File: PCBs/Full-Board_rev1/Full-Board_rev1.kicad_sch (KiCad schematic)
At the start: 1 part, among them U1 ESP32-C6-WROOM-1

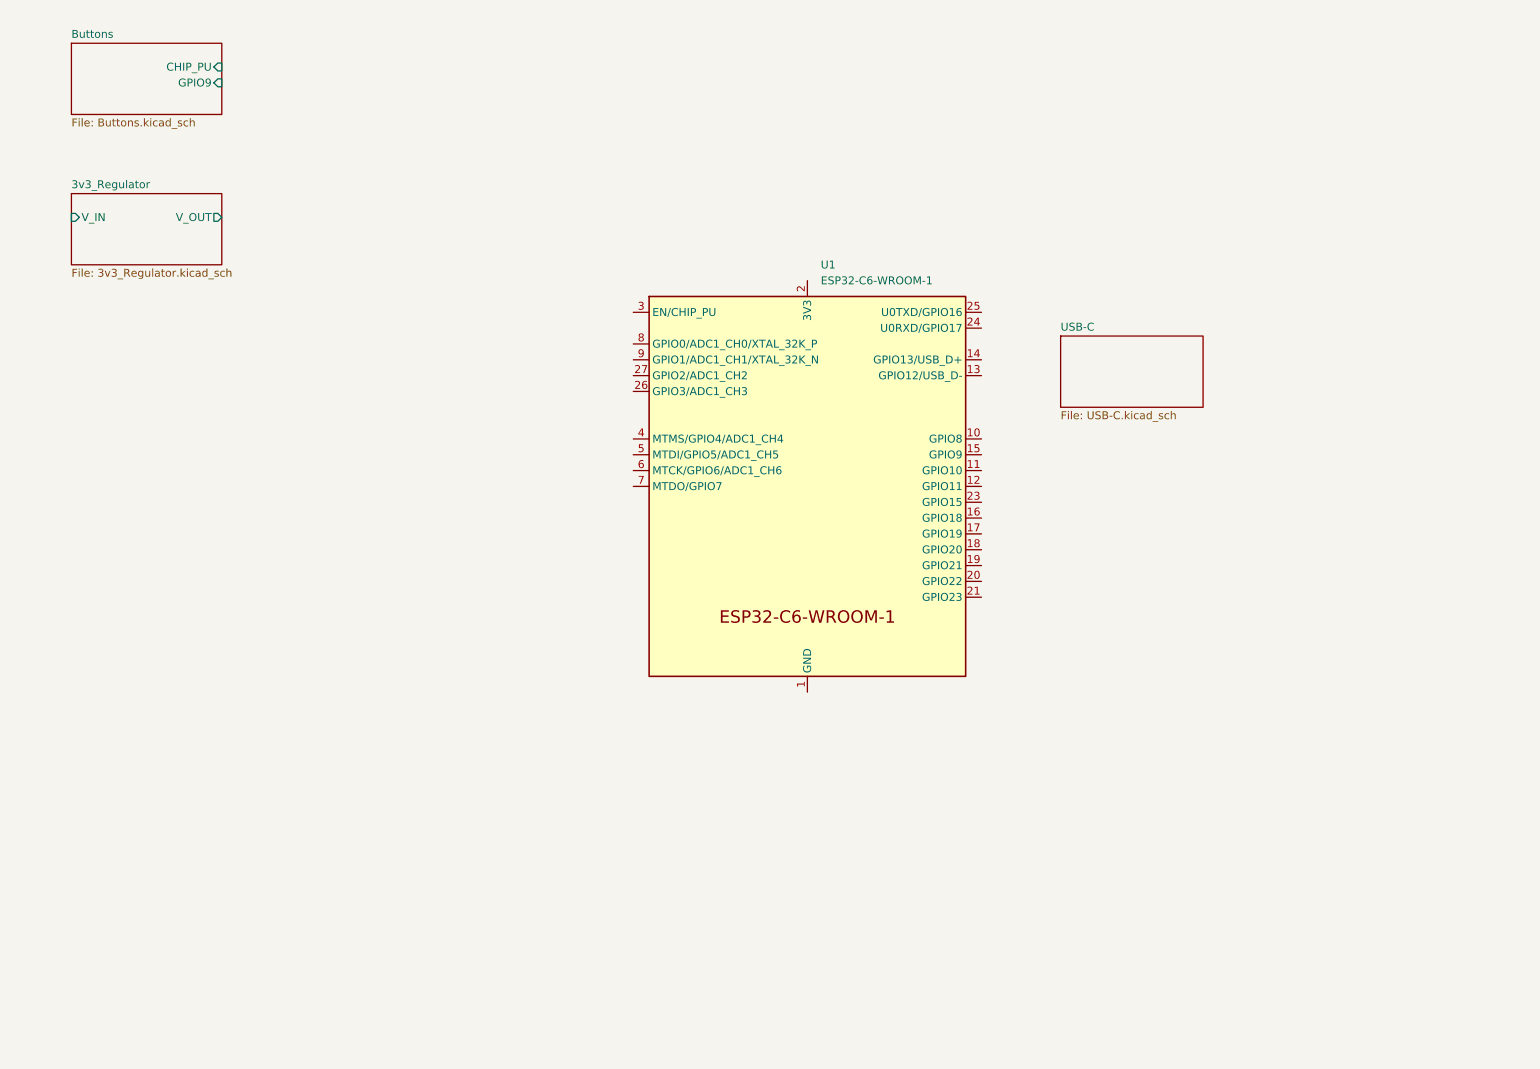
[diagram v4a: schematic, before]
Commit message: added ESP32 peripherals
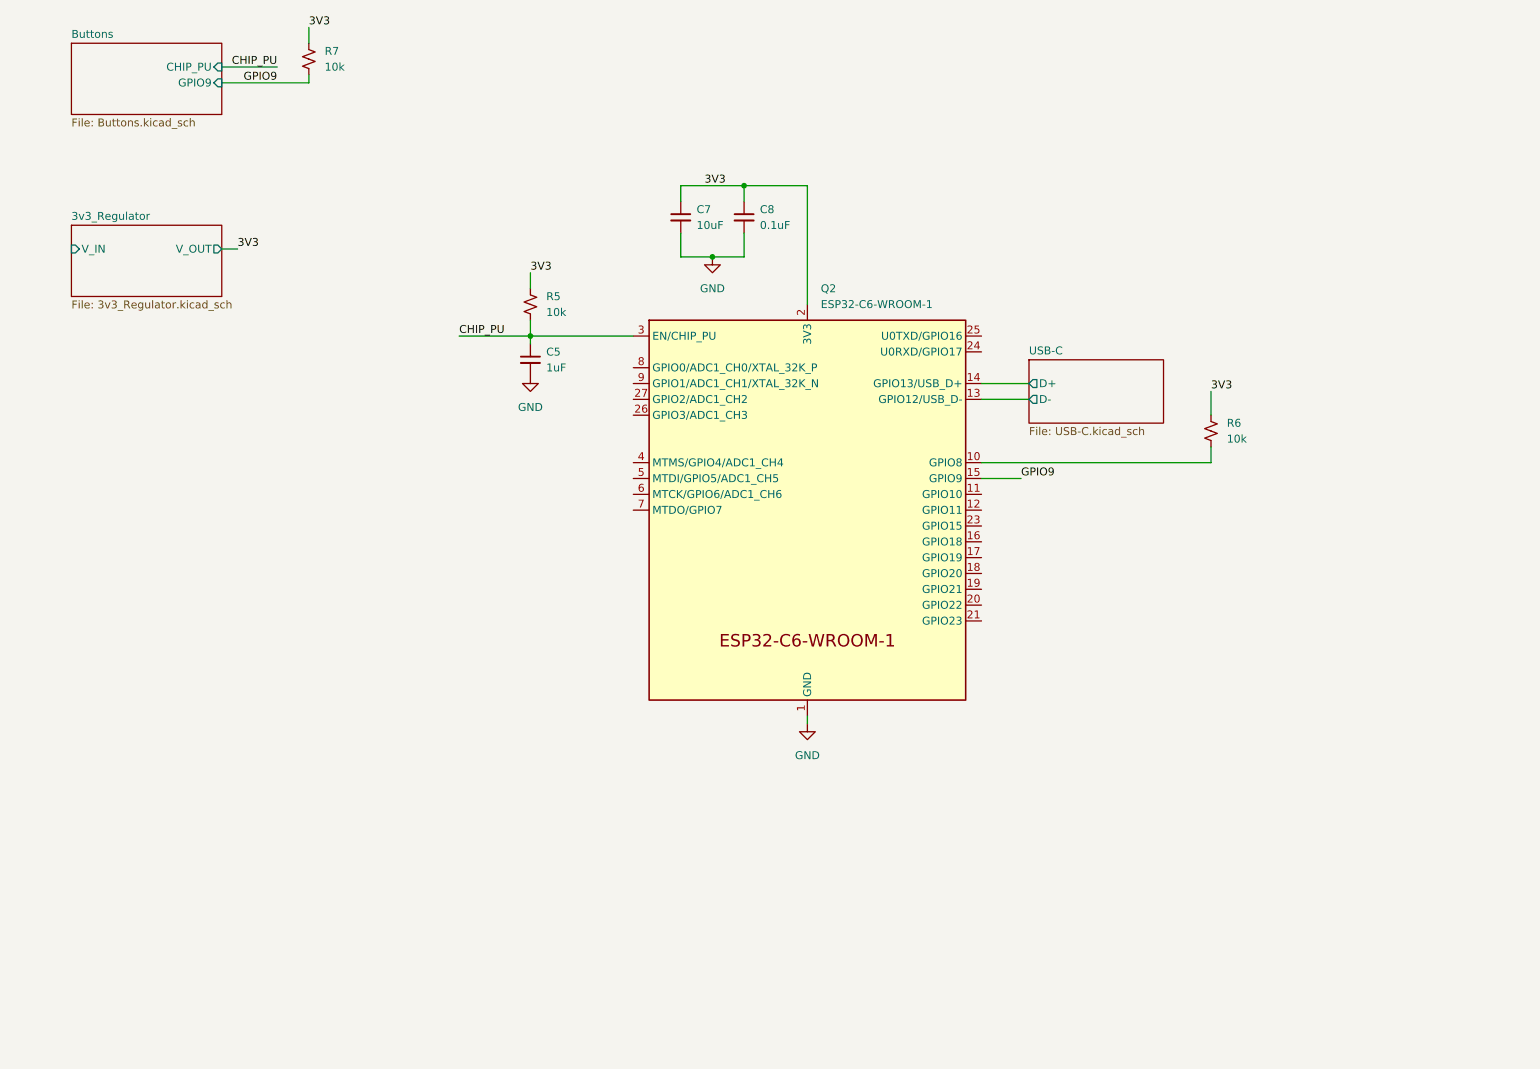
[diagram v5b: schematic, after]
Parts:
- added C5: 1uF, symbol Device:C_Small
- added C7: 10uF, symbol Device:C_Small
- added C8: 0.1uF, symbol Device:C_Small
- added R5, R6, R7: 10k, symbol Device:R_Small_US
- renumbered U1 to Q2
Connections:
- net GND: now reaches Q2.1 (GND), Q2.28 (GND), Q2.29 (GND)
- net GND: now also C5.2, C7.2, C8.2
- net at Q2.10 (GPIO8): now also R6.2
- net USB-C/D-: now reaches Q2.13 (GPIO12/USB_D-)
- net USB-C/D+: now reaches Q2.14 (GPIO13/USB_D+)
- net GPIO9: now reaches Q2.15 (GPIO9)
- net GPIO9: now also R7.2
- net 3V3: now reaches Q2.2 (3V3)
- net 3V3: now also C7.1, C8.1, R5.1, R6.1, R7.1
- net CHIP_PU: now reaches Q2.3 (EN/CHIP_PU)
- net CHIP_PU: now also C5.1, R5.2
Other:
- sheet USB-C ports: added D+, D-; removed none
- moved on the sheet: Q2

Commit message: LEDs added
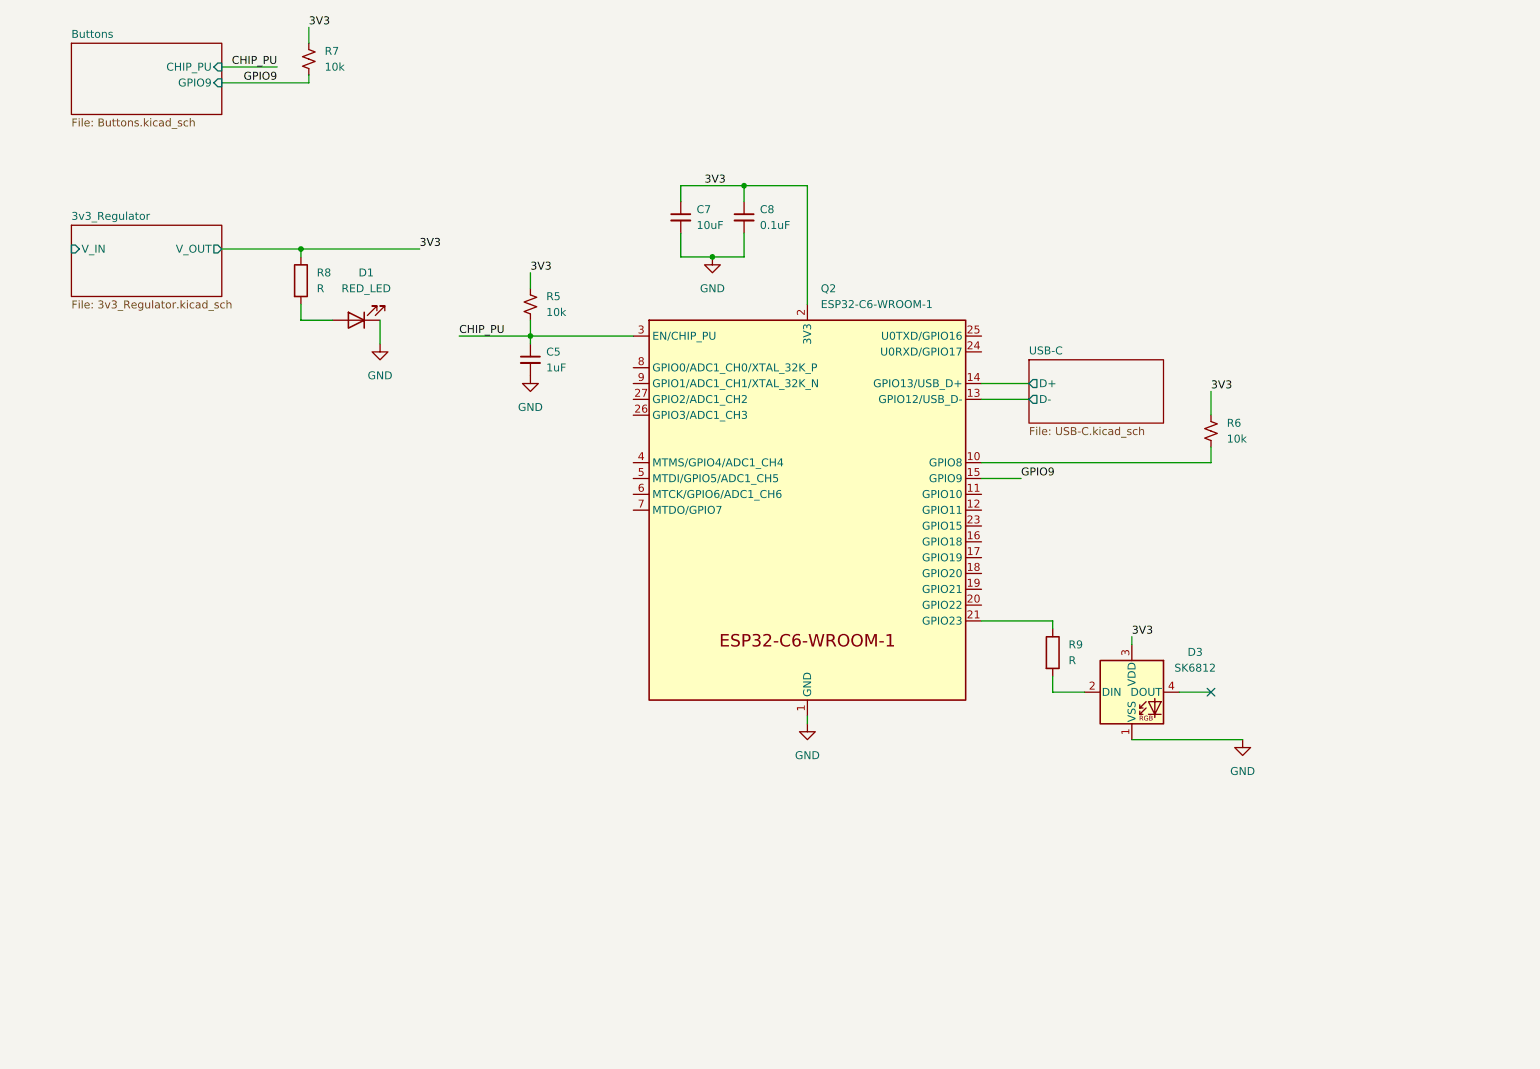
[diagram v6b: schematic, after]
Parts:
- added D1: RED_LED, symbol Device:LED
- added D3: SK6812, LED_SMD:LED_SK6812_PLCC4_5.0x5.0mm_P3.2mm, symbol LED:SK6812
- added R8, R9: R, symbol Device:R
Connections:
- net 3V3: now also D3.3 (VDD), R8.1
- net GND: now also D1.1 (K), D3.1 (VSS)
- net at Q2.21 (GPIO23): now also R9.1
- new net: D1.2 (A), R8.2
- new net: D3.2 (DIN), R9.2
- no-connect marks 0 -> 1

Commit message: Motor driver, motor+encoder headers added
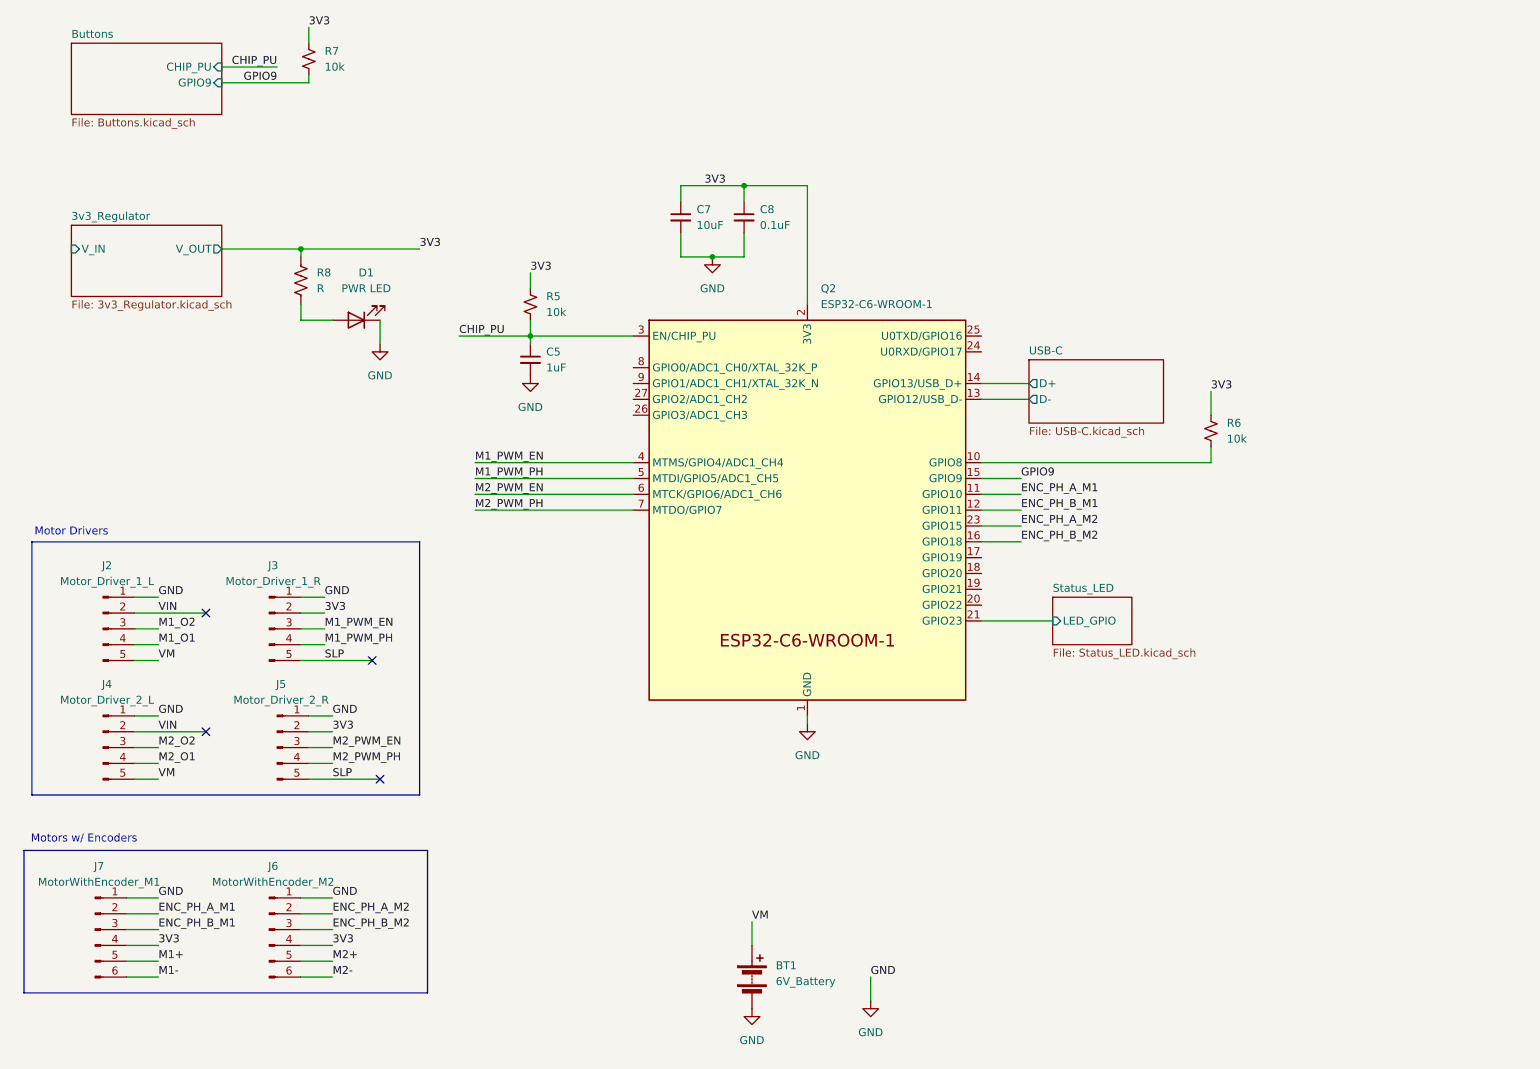
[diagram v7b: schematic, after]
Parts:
- removed D3: SK6812, LED_SMD:LED_SK6812_PLCC4_5.0x5.0mm_P3.2mm, symbol LED:SK6812
- removed R9: R, symbol Device:R
- added BT1: 6V_Battery, symbol Device:Battery
- added J2: Motor_Driver_1_L, symbol Connector:Conn_01x05_Pin
- added J3: Motor_Driver_1_R, symbol Connector:Conn_01x05_Pin
- added J4: Motor_Driver_2_L, symbol Connector:Conn_01x05_Pin
- added J5: Motor_Driver_2_R, symbol Connector:Conn_01x05_Pin
- added J6: MotorWithEncoder_M2, symbol Connector:Conn_01x06_Pin
- added J7: MotorWithEncoder_M1, symbol Connector:Conn_01x06_Pin
- D1: value RED_LED -> PWR LED
- R8: symbol Device:R -> Device:R_US
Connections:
- net 3V3: now also J3.2 (Pin_2), J5.2 (Pin_2), J6.4 (Pin_4), J7.4 (Pin_4)
- net GND: now also BT1.2 (-), J2.1 (Pin_1), J3.1 (Pin_1), J4.1 (Pin_1), J5.1 (Pin_1), J6.1 (Pin_1), J7.1 (Pin_1)
- net ENC_PH_A_M1: now reaches Q2.11 (GPIO10)
- net ENC_PH_A_M1: now also J7.2 (Pin_2)
- net ENC_PH_B_M1: now reaches Q2.12 (GPIO11)
- net ENC_PH_B_M1: now also J7.3 (Pin_3)
- net ENC_PH_B_M2: now reaches Q2.16 (GPIO18)
- net ENC_PH_B_M2: now also J6.3 (Pin_3)
- net Status_LED/LED_GPIO: now reaches Q2.21 (GPIO23)
- net ENC_PH_A_M2: now reaches Q2.23 (GPIO15)
- net ENC_PH_A_M2: now also J6.2 (Pin_2)
- net M1_PWM_EN: now reaches Q2.4 (MTMS/GPIO4/ADC1_CH4)
- net M1_PWM_EN: now also J3.3 (Pin_3)
- net M1_PWM_PH: now reaches Q2.5 (MTDI/GPIO5/ADC1_CH5)
- net M1_PWM_PH: now also J3.4 (Pin_4)
- net M2_PWM_EN: now reaches Q2.6 (MTCK/GPIO6/ADC1_CH6)
- net M2_PWM_EN: now also J5.3 (Pin_3)
- net M2_PWM_PH: now reaches Q2.7 (MTDO/GPIO7)
- net M2_PWM_PH: now also J5.4 (Pin_4)
- new net M1+: J7.5 (Pin_5)
- new net M1-: J7.6 (Pin_6)
- new net M1_O1: J2.4 (Pin_4)
- new net M1_O2: J2.3 (Pin_3)
- new net M2+: J6.5 (Pin_5)
- new net M2-: J6.6 (Pin_6)
- new net M2_O1: J4.4 (Pin_4)
- new net M2_O2: J4.3 (Pin_3)
- new net SLP: J3.5 (Pin_5), J5.5 (Pin_5)
- new net VIN: J2.2 (Pin_2), J4.2 (Pin_2)
- new net VM: BT1.1 (+), J2.5 (Pin_5), J4.5 (Pin_5)
- no-connect marks 1 -> 4
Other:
- added sheet Status_LED (Status_LED.kicad_sch)
- note added: "Motor Drivers"
- note added: "Motors w/ Encoders"

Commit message: Adjusted and Added headers to schematic
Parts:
- removed BT1: 6V_Battery, symbol Device:Battery
- removed J2: Motor_Driver_1_L, symbol Connector:Conn_01x05_Pin
- removed J3: Motor_Driver_1_R, symbol Connector:Conn_01x05_Pin
- removed J4: Motor_Driver_2_L, symbol Connector:Conn_01x05_Pin
- removed J5: Motor_Driver_2_R, symbol Connector:Conn_01x05_Pin
- added J10: Conn_01x11, symbol Connector_Generic:Conn_01x11
- added J2, J3, J4, J5: Conn_01x05, symbol Connector_Generic:Conn_01x05
- added J8, J9: Conn_01x02, symbol Connector_Generic:Conn_01x02
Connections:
- net M1+ is gone; now on net M1_O1: J7.5 (Pin_5)
- net M1- is gone; now on net M1_O2: J7.6 (Pin_6)
- net M2+ is gone; now on net M2_O1: J6.5 (Pin_5)
- net M2- is gone; now on net M2_O2: J6.6 (Pin_6)
- net 3V3: now also J10.2 (Pin_2), J3.2 (Pin_2), J4.2 (Pin_2)
- net ENC_PH_A_M1: now also Q2.8 (GPIO0/ADC1_CH0/XTAL_32K_P); no longer Q2.11 (GPIO10)
- net ENC_PH_A_M2: now also Q2.27 (GPIO2/ADC1_CH2); no longer Q2.23 (GPIO15)
- net ENC_PH_B_M1: now also Q2.9 (GPIO1/ADC1_CH1/XTAL_32K_N); no longer Q2.12 (GPIO11)
- net ENC_PH_B_M2: now also Q2.26 (GPIO3/ADC1_CH3); no longer Q2.16 (GPIO18)
- net GND: now also J10.1 (Pin_1), J2.1 (Pin_1), J3.1 (Pin_1), J4.1 (Pin_1), J5.1 (Pin_1), J8.2 (Pin_2), J9.2 (Pin_2)
- net M1_O1: now also J2.4 (Pin_4)
- net M1_O2: now also J2.3 (Pin_3)
- net M1_PWM_EN: now also J3.3 (Pin_3)
- net M1_PWM_PH: now also J3.4 (Pin_4)
- net M2_O1: now also J5.4 (Pin_4)
- net M2_O2: now also J5.3 (Pin_3)
- net M2_PWM_EN: now also J4.3 (Pin_3)
- net M2_PWM_PH: now also J4.4 (Pin_4)
- net VIN: now also J9.1 (Pin_1)
- net IR_O5: now reaches Q2.17 (GPIO19)
- net IR_O5: now also J10.8 (Pin_8)
- net IR_O6: now reaches Q2.18 (GPIO20)
- net IR_O6: now also J10.9 (Pin_9)
- net IR_O7: now reaches Q2.19 (GPIO21)
- net IR_O7: now also J10.10 (Pin_10)
- net IR_O8: now reaches Q2.20 (GPIO22)
- net IR_O8: now also J10.11 (Pin_11)
- new net 6V: J2.2 (Pin_2), J5.2 (Pin_2), J8.1 (Pin_1)
- new net IR_O1: J10.4 (Pin_4), Q2.11 (GPIO10)
- new net IR_O2: J10.5 (Pin_5), Q2.12 (GPIO11)
- new net IR_O3: J10.6 (Pin_6), Q2.23 (GPIO15)
- new net IR_O4: J10.7 (Pin_7), Q2.16 (GPIO18)
- no-connect marks 4 -> 5
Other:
- note added: "6 AA Battery Pack"
- note added: "CTRL"
- note added: "IR Sensor Array"
- note added: "LiIon Battery"
- note added: "M1+"
- note added: "M1-"
- note added: "M2+"
- note added: "M2-"
- note added: "SLEEP"
- note added: "VMM"
- moved on the sheet: C5, R5
